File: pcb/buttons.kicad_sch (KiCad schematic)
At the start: 17 parts, among them J7 External FG-One, J8 External FG-Flex, SW1 FG-Flex Button, SW1 FG-One Button, U11 74HC14

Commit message: more stuff corrected
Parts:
- added C11: 0.1uF, Capacitor_THT:C_Disc_D5.1mm_W3.2mm_P5.00mm, symbol Device:C_Small
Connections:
- net GND: now also U11.11, U11.13, U11.7 (GND), C11.2
- net +5V: now reaches U11.14 (VCC)
- net +5V: now also C11.1
- no-connect marks 0 -> 2
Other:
- title: (none) -> Button
- moved on the sheet: U11E, U11F, U11G

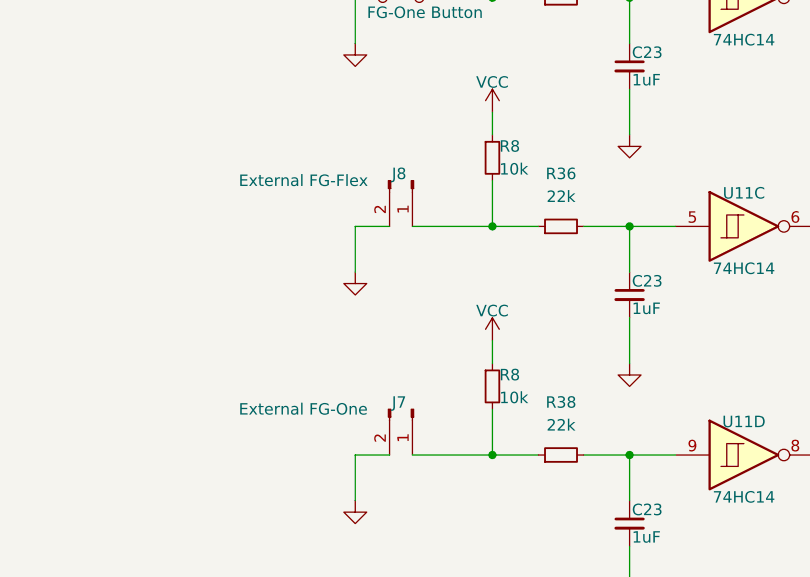
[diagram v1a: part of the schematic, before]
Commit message: potentiometer to set pwm for warm and cold light added
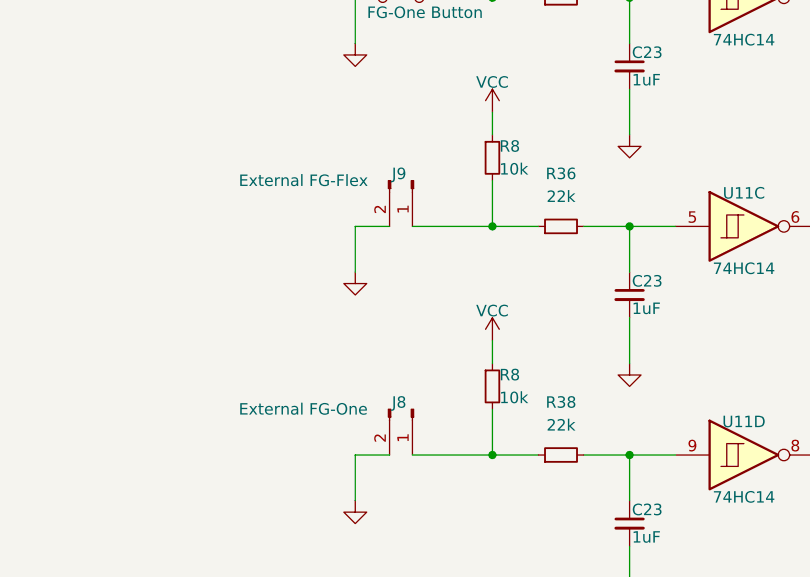
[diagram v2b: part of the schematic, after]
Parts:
- renumbered J7 to J8, J8 to J9
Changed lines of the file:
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@@
   (title_block
     (title "Button")
-    (date "2023-11-16")
+    (date "2023-11-22")
     (rev "0.2")
   )
@@
   (symbol (lib_id "Connector:Conn_01x02_Pin") (at 146.05 96.52 270) (unit 1)
     (in_bom yes) (on_board yes) (dnp no)
-    (property "Reference" "J8" (at 143.764 95.758 90)
+    (property "Reference" "J9" (at 143.764 95.758 90)
       (effects (font (size 1.27 1.27)) (justify left))
     )
@@
       (project "fg_lampe"
         (path "/6ce7d73a-8297-412b-a1cf-6113d41486fd/4a5818b1-c178-488d-ac41-3ad29eecedbe"
-          (reference "J8") (unit 1)
+          (reference "J9") (unit 1)
         )
       )
@@
   (symbol (lib_id "Connector:Conn_01x02_Pin") (at 146.05 121.92 270) (unit 1)
     (in_bom yes) (on_board yes) (dnp no)
-    (property "Reference" "J7" (at 143.764 121.158 90)
+    (property "Reference" "J8" (at 143.764 121.158 90)
       (effects (font (size 1.27 1.27)) (justify left))
     )
@@
       (project "fg_lampe"
         (path "/6ce7d73a-8297-412b-a1cf-6113d41486fd/4a5818b1-c178-488d-ac41-3ad29eecedbe"
-          (reference "J7") (unit 1)
-        )
-      )
+          (reference "J8") (unit 1)
+        )
+      )

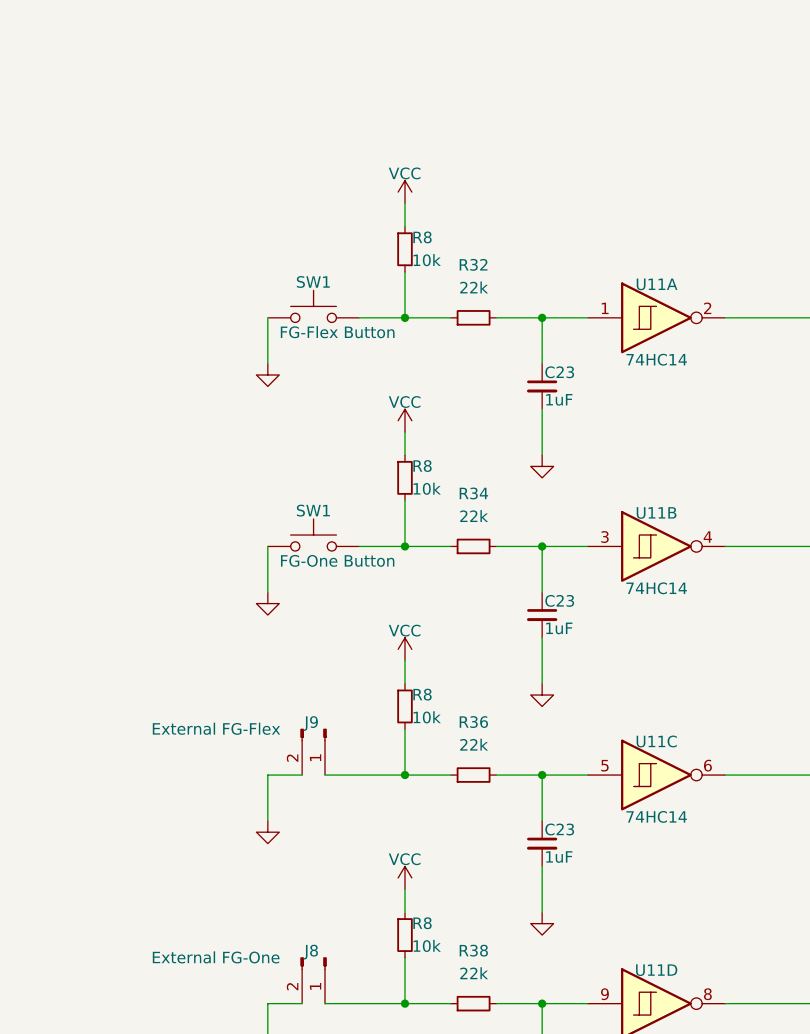
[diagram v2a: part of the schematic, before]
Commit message: vcc changed with +24V
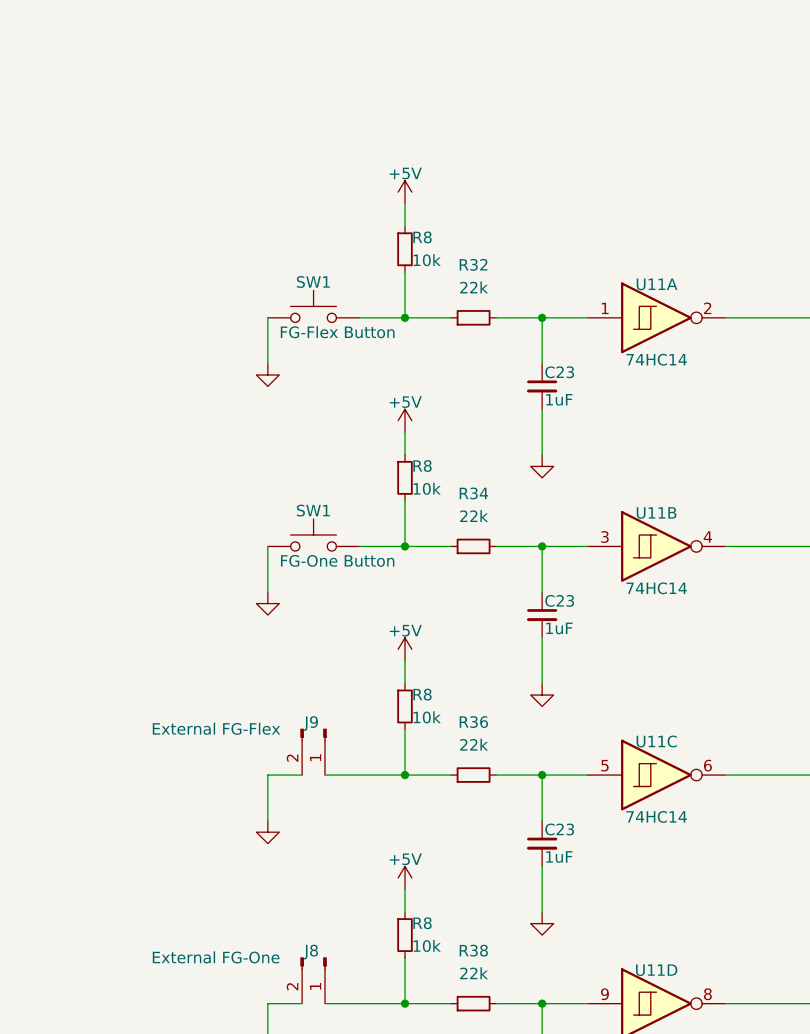
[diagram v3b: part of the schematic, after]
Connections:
- net VCC is gone; now on net +5V: R8.1, R8.1, R8.1, R8.1

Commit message: minor changes
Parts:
- J8, J9: footprint (none) -> Connector_JST:JST_EH_B2B-EH-A_1x02_P2.50mm_Vertical
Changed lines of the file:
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@@
       (effects (font (size 1.27 1.27)) (justify left))
     )
-    (property "Footprint" "" (at 146.05 96.52 0)
+    (property "Footprint" "Connector_JST:JST_EH_B2B-EH-A_1x02_P2.50mm_Vertical" (at 146.05 96.52 0)
       (effects (font (size 1.27 1.27)) hide)
     )
@@
       (effects (font (size 1.27 1.27)) (justify left))
     )
-    (property "Footprint" "" (at 146.05 121.92 0)
-      (effects (font (size 1.27 1.27)) hide)
-    )
+    (property "Footprint" "Connector_JST:JST_EH_B2B-EH-A_1x02_P2.50mm_Vertical" (at 146.05 121.92 0)
+      (effects (font (size 1.27 1.27)) hide)
+    )

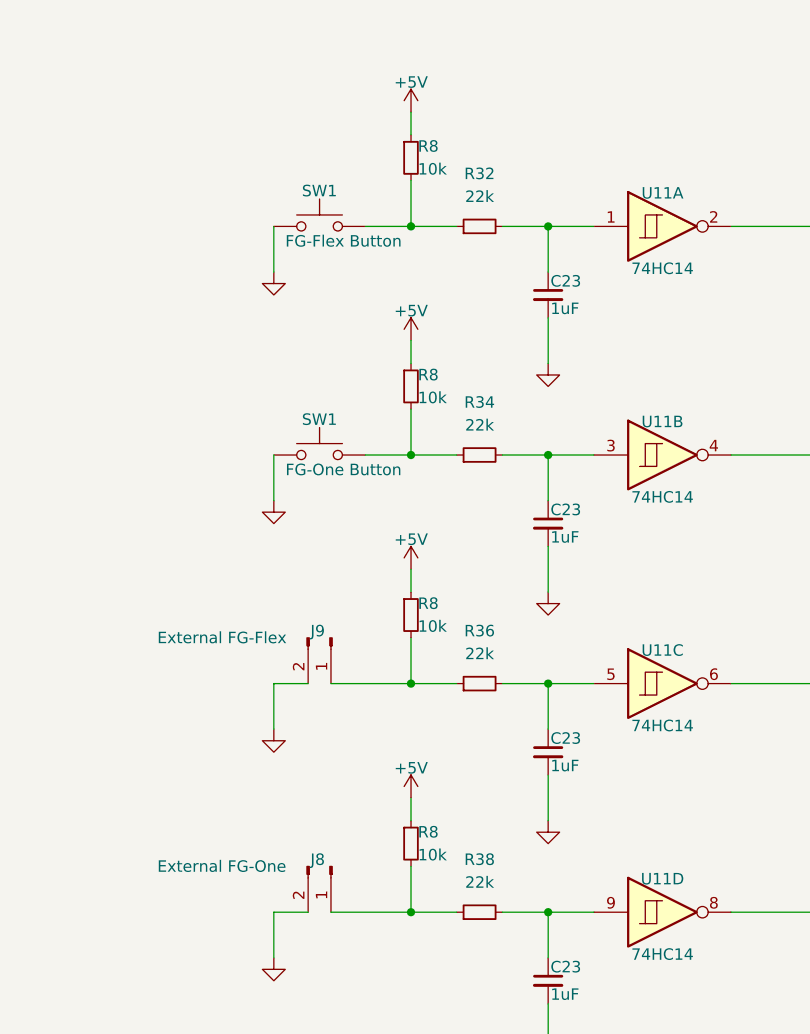
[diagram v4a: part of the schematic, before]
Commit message: sma measurement added, new connector for leds, some minor fixes
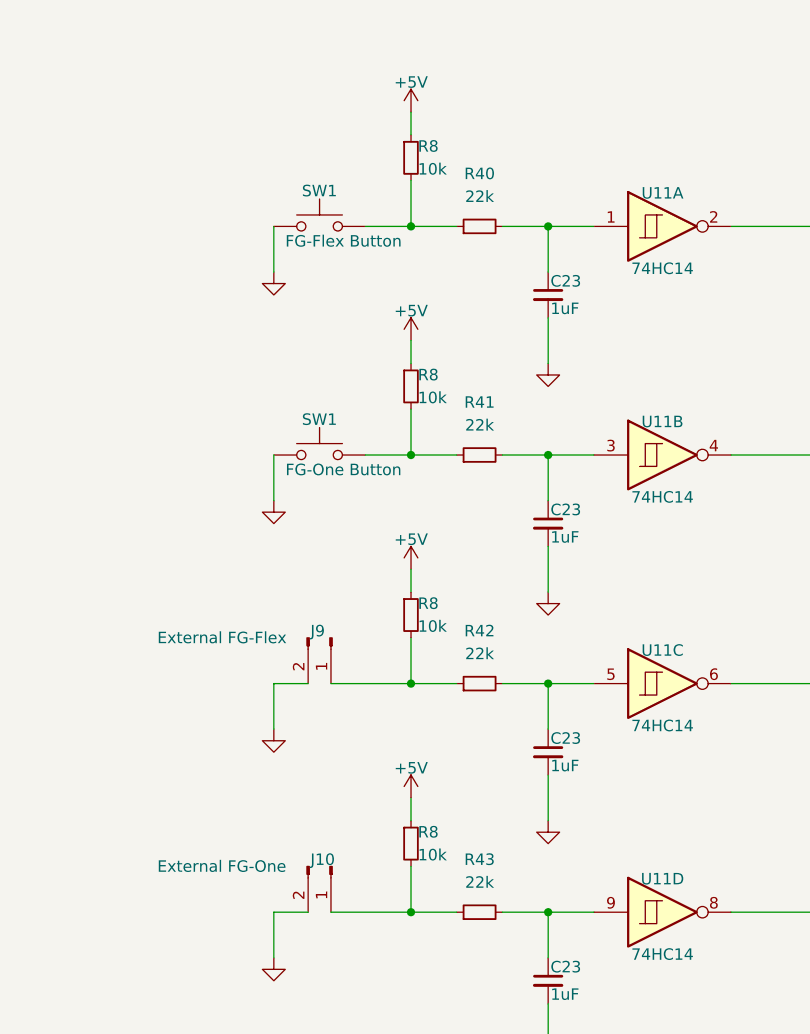
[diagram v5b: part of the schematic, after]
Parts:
- renumbered J8 to J10, R32 to R40, R34 to R41, R36 to R42, R38 to R43
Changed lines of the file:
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@@
         )
         (path "/6ce7d73a-8297-412b-a1cf-6113d41486fd/4a5818b1-c178-488d-ac41-3ad29eecedbe"
-          (reference "C27") (unit 1)
+          (reference "C34") (unit 1)
         )
       )
@@
         )
         (path "/6ce7d73a-8297-412b-a1cf-6113d41486fd/4a5818b1-c178-488d-ac41-3ad29eecedbe"
-          (reference "R33") (unit 1)
+          (reference "R37") (unit 1)
         )
       )
@@
   (symbol (lib_id "Device:R_Small") (at 162.56 127 90) (unit 1)
     (in_bom yes) (on_board yes) (dnp no) (fields_autoplaced)
-    (property "Reference" "R38" (at 162.56 121.158 90)
+    (property "Reference" "R43" (at 162.56 121.158 90)
       (effects (font (size 1.27 1.27)))
     )
@@
       (project "fg_lampe"
         (path "/6ce7d73a-8297-412b-a1cf-6113d41486fd/4a5818b1-c178-488d-ac41-3ad29eecedbe"
-          (reference "R38") (unit 1)
+          (reference "R43") (unit 1)
         )
       )
@@
         )
         (path "/6ce7d73a-8297-412b-a1cf-6113d41486fd/4a5818b1-c178-488d-ac41-3ad29eecedbe"
-          (reference "U11") (unit 6)
+          (reference "U12") (unit 6)
         )
       )
@@
         )
         (path "/6ce7d73a-8297-412b-a1cf-6113d41486fd/4a5818b1-c178-488d-ac41-3ad29eecedbe"
-          (reference "C23") (unit 1)
+          (reference "C30") (unit 1)
         )
       )
@@
   (symbol (lib_id "Device:R_Small") (at 162.56 76.2 90) (unit 1)
     (in_bom yes) (on_board yes) (dnp no) (fields_autoplaced)
-    (property "Reference" "R34" (at 162.56 70.358 90)
+    (property "Reference" "R41" (at 162.56 70.358 90)
       (effects (font (size 1.27 1.27)))
     )
@@
       (project "fg_lampe"
         (path "/6ce7d73a-8297-412b-a1cf-6113d41486fd/4a5818b1-c178-488d-ac41-3ad29eecedbe"
-          (reference "R34") (unit 1)
+          (reference "R41") (unit 1)
         )
       )
@@
         )
         (path "/6ce7d73a-8297-412b-a1cf-6113d41486fd/4a5818b1-c178-488d-ac41-3ad29eecedbe"
-          (reference "U11") (unit 3)
+          (reference "U12") (unit 3)
         )
       )
@@
         )
         (path "/6ce7d73a-8297-412b-a1cf-6113d41486fd/4a5818b1-c178-488d-ac41-3ad29eecedbe"
-          (reference "#PWR095") (unit 1)
+          (reference "#PWR0126") (unit 1)
         )
       )
@@
         )
         (path "/6ce7d73a-8297-412b-a1cf-6113d41486fd/4a5818b1-c178-488d-ac41-3ad29eecedbe"
-          (reference "#PWR0100") (unit 1)
+          (reference "#PWR0113") (unit 1)
         )
       )
@@
         )
         (path "/6ce7d73a-8297-412b-a1cf-6113d41486fd/4a5818b1-c178-488d-ac41-3ad29eecedbe"
-          (reference "#PWR088") (unit 1)
+          (reference "#PWR0121") (unit 1)
         )
       )
@@
         )
         (path "/6ce7d73a-8297-412b-a1cf-6113d41486fd/4a5818b1-c178-488d-ac41-3ad29eecedbe"
-          (reference "U11") (unit 1)
+          (reference "U12") (unit 1)
         )
       )
@@
         )
         (path "/6ce7d73a-8297-412b-a1cf-6113d41486fd/4a5818b1-c178-488d-ac41-3ad29eecedbe"
-          (reference "R37") (unit 1)
+          (reference "R39") (unit 1)
         )
       )
@@
         )
         (path "/6ce7d73a-8297-412b-a1cf-6113d41486fd/4a5818b1-c178-488d-ac41-3ad29eecedbe"
-          (reference "U11") (unit 5)
+          (reference "U12") (unit 5)
         )
       )
@@
         )
         (path "/6ce7d73a-8297-412b-a1cf-6113d41486fd/4a5818b1-c178-488d-ac41-3ad29eecedbe"
-          (reference "#PWR086") (unit 1)
+          (reference "#PWR0123") (unit 1)
         )
       )
@@
         )
         (path "/6ce7d73a-8297-412b-a1cf-6113d41486fd/4a5818b1-c178-488d-ac41-3ad29eecedbe"
-          (reference "C24") (unit 1)
+          (reference "C31") (unit 1)
         )
       )
@@
         )
         (path "/6ce7d73a-8297-412b-a1cf-6113d41486fd/4a5818b1-c178-488d-ac41-3ad29eecedbe"
-          (reference "C25") (unit 1)
+          (reference "C32") (unit 1)
         )
       )
@@
         )
         (path "/6ce7d73a-8297-412b-a1cf-6113d41486fd/4a5818b1-c178-488d-ac41-3ad29eecedbe"
-          (reference "R35") (unit 1)
+          (reference "R38") (unit 1)
         )
       )
@@
         )
         (path "/6ce7d73a-8297-412b-a1cf-6113d41486fd/4a5818b1-c178-488d-ac41-3ad29eecedbe"
-          (reference "U11") (unit 2)
+          (reference "U12") (unit 2)
         )
       )
@@
         )
         (path "/6ce7d73a-8297-412b-a1cf-6113d41486fd/4a5818b1-c178-488d-ac41-3ad29eecedbe"
-          (reference "#PWR090") (unit 1)
+          (reference "#PWR0117") (unit 1)
         )
       )
@@
         )
         (path "/6ce7d73a-8297-412b-a1cf-6113d41486fd/4a5818b1-c178-488d-ac41-3ad29eecedbe"
-          (reference "#PWR096") (unit 1)
+          (reference "#PWR0127") (unit 1)
         )
       )
@@
         )
         (path "/6ce7d73a-8297-412b-a1cf-6113d41486fd/4a5818b1-c178-488d-ac41-3ad29eecedbe"
-          (reference "#PWR097") (unit 1)
+          (reference "#PWR0128") (unit 1)
         )
       )
@@
         )
         (path "/6ce7d73a-8297-412b-a1cf-6113d41486fd/4a5818b1-c178-488d-ac41-3ad29eecedbe"
-          (reference "#PWR099") (unit 1)
+          (reference "#PWR0129") (unit 1)
         )
       )
@@
         )
         (path "/6ce7d73a-8297-412b-a1cf-6113d41486fd/4a5818b1-c178-488d-ac41-3ad29eecedbe"
-          (reference "#PWR089") (unit 1)
+          (reference "#PWR0124") (unit 1)
         )
       )
@@
         )
         (path "/6ce7d73a-8297-412b-a1cf-6113d41486fd/4a5818b1-c178-488d-ac41-3ad29eecedbe"
-          (reference "#PWR0101") (unit 1)
+          (reference "#PWR0114") (unit 1)
         )
       )
@@
         )
         (path "/6ce7d73a-8297-412b-a1cf-6113d41486fd/4a5818b1-c178-488d-ac41-3ad29eecedbe"
-          (reference "C26") (unit 1)
+          (reference "C33") (unit 1)
         )
       )
@@
         )
         (path "/6ce7d73a-8297-412b-a1cf-6113d41486fd/4a5818b1-c178-488d-ac41-3ad29eecedbe"
-          (reference "#PWR048") (unit 1)
+          (reference "#PWR0119") (unit 1)
         )
       )
@@
         )
         (path "/6ce7d73a-8297-412b-a1cf-6113d41486fd/4a5818b1-c178-488d-ac41-3ad29eecedbe"
-          (reference "#PWR085") (unit 1)
+          (reference "#PWR0115") (unit 1)
         )
       )
@@
         )
         (path "/6ce7d73a-8297-412b-a1cf-6113d41486fd/4a5818b1-c178-488d-ac41-3ad29eecedbe"
-          (reference "R31") (unit 1)
+          (reference "R36") (unit 1)
         )
       )
@@
         )
         (path "/6ce7d73a-8297-412b-a1cf-6113d41486fd/4a5818b1-c178-488d-ac41-3ad29eecedbe"
-          (reference "U11") (unit 7)
+          (reference "U12") (unit 7)
         )
       )
@@
         )
         (path "/6ce7d73a-8297-412b-a1cf-6113d41486fd/4a5818b1-c178-488d-ac41-3ad29eecedbe"
-          (reference "U11") (unit 4)
+          (reference "U12") (unit 4)
         )
       )
@@
         )
         (path "/6ce7d73a-8297-412b-a1cf-6113d41486fd/4a5818b1-c178-488d-ac41-3ad29eecedbe"
-          (reference "#PWR087") (unit 1)
+          (reference "#PWR0116") (unit 1)
         )
       )
@@
   (symbol (lib_id "Connector:Conn_01x02_Pin") (at 146.05 121.92 270) (unit 1)
     (in_bom yes) (on_board yes) (dnp no)
-    (property "Reference" "J8" (at 143.764 121.158 90)
+    (property "Reference" "J10" (at 143.764 121.158 90)
       (effects (font (size 1.27 1.27)) (justify left))
     )
@@
       (project "fg_lampe"
         (path "/6ce7d73a-8297-412b-a1cf-6113d41486fd/4a5818b1-c178-488d-ac41-3ad29eecedbe"
-          (reference "J8") (unit 1)
+          (reference "J10") (unit 1)
         )
       )
@@
         )
         (path "/6ce7d73a-8297-412b-a1cf-6113d41486fd/4a5818b1-c178-488d-ac41-3ad29eecedbe"
-          (reference "#PWR092") (unit 1)
+          (reference "#PWR0125") (unit 1)
         )
       )
@@
   (symbol (lib_id "Device:R_Small") (at 162.56 50.8 90) (unit 1)
     (in_bom yes) (on_board yes) (dnp no) (fields_autoplaced)
-    (property "Reference" "R32" (at 162.56 44.958 90)
+    (property "Reference" "R40" (at 162.56 44.958 90)
       (effects (font (size 1.27 1.27)))
     )
@@
       (project "fg_lampe"
         (path "/6ce7d73a-8297-412b-a1cf-6113d41486fd/4a5818b1-c178-488d-ac41-3ad29eecedbe"
-          (reference "R32") (unit 1)
+          (reference "R40") (unit 1)
         )
       )
@@
         )
         (path "/6ce7d73a-8297-412b-a1cf-6113d41486fd/4a5818b1-c178-488d-ac41-3ad29eecedbe"
-          (reference "#PWR093") (unit 1)
+          (reference "#PWR0118") (unit 1)
         )
       )
@@
         )
         (path "/6ce7d73a-8297-412b-a1cf-6113d41486fd/4a5818b1-c178-488d-ac41-3ad29eecedbe"
-          (reference "#PWR084") (unit 1)
+          (reference "#PWR0120") (unit 1)
         )
       )
@@
   (symbol (lib_id "Device:R_Small") (at 162.56 101.6 90) (unit 1)
     (in_bom yes) (on_board yes) (dnp no) (fields_autoplaced)
-    (property "Reference" "R36" (at 162.56 95.758 90)
+    (property "Reference" "R42" (at 162.56 95.758 90)
       (effects (font (size 1.27 1.27)))
     )
@@
       (project "fg_lampe"
         (path "/6ce7d73a-8297-412b-a1cf-6113d41486fd/4a5818b1-c178-488d-ac41-3ad29eecedbe"
-          (reference "R36") (unit 1)
+          (reference "R42") (unit 1)
         )
       )
@@
         )
         (path "/6ce7d73a-8297-412b-a1cf-6113d41486fd/4a5818b1-c178-488d-ac41-3ad29eecedbe"
-          (reference "#PWR091") (unit 1)
+          (reference "#PWR0122") (unit 1)
         )
       )
@@
         )
         (path "/6ce7d73a-8297-412b-a1cf-6113d41486fd/4a5818b1-c178-488d-ac41-3ad29eecedbe"
-          (reference "#PWR098") (unit 1)
-        )
-      )
+          (reference "#PWR0130") (unit 1)
+        )
+      )

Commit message: final version schematic?
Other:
- company: (none) -> /dev/tal e.V.
- title: Button -> Buttons and Inverters
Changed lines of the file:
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@@
   (paper "A4")
   (title_block
-    (title "Button")
-    (date "2023-11-22")
-    (rev "0.2")
+    (title "Buttons and Inverters")
+    (date "2023-12-09")
+    (rev "0.5")
+    (company "/dev/tal e.V.")
   )
   (junction (at 170.18 50.8) (diameter 0) (color 0 0 0 0)

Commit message: finals in schematic
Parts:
- C11: footprint Capacitor_THT:C_Disc_D5.1mm_W3.2mm_P5.00mm -> Capacitor_THT:C_Disc_D5.0mm_W2.5mm_P2.50mm
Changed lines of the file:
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@@
       (effects (font (size 1.27 1.27)) (justify left))
     )
-    (property "Footprint" "Capacitor_THT:C_Disc_D5.1mm_W3.2mm_P5.00mm" (at 236.22 38.1 0)
+    (property "Footprint" "Capacitor_THT:C_Disc_D5.0mm_W2.5mm_P2.50mm" (at 236.22 38.1 0)
       (effects (font (size 1.27 1.27)) hide)
     )
